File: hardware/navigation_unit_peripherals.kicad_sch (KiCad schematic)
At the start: 25 parts, among them J1 RFPC-SMA28-F, J2 Conn_01x04, U2 BMI088, U3 IIS2MDCTR, U4 MPRLS0025PA00001A, U5 TMP100, U6 24CW1280T-I/OT, U7 MAX-M8Q

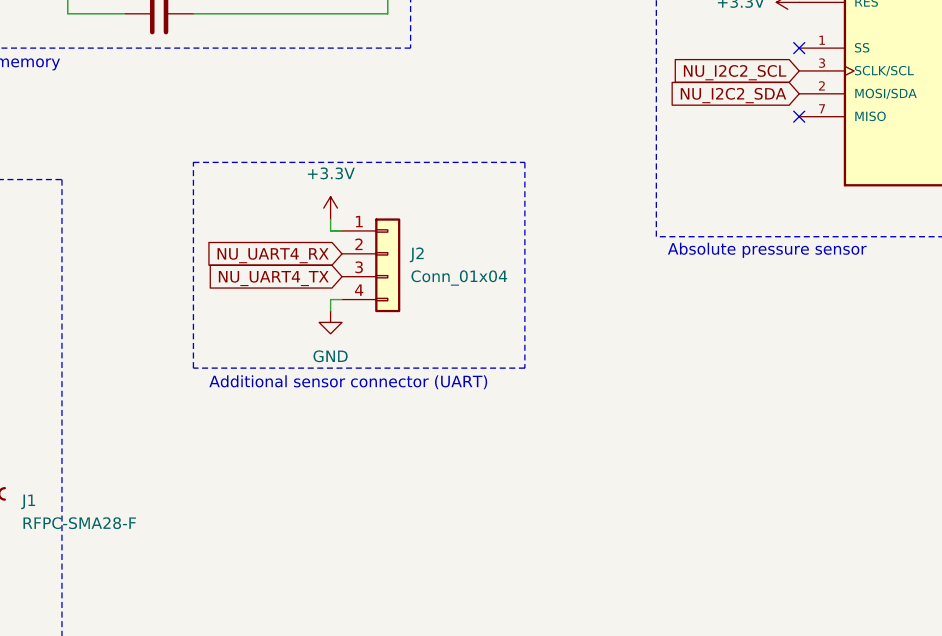
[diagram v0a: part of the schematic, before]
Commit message: schematic and BOM done
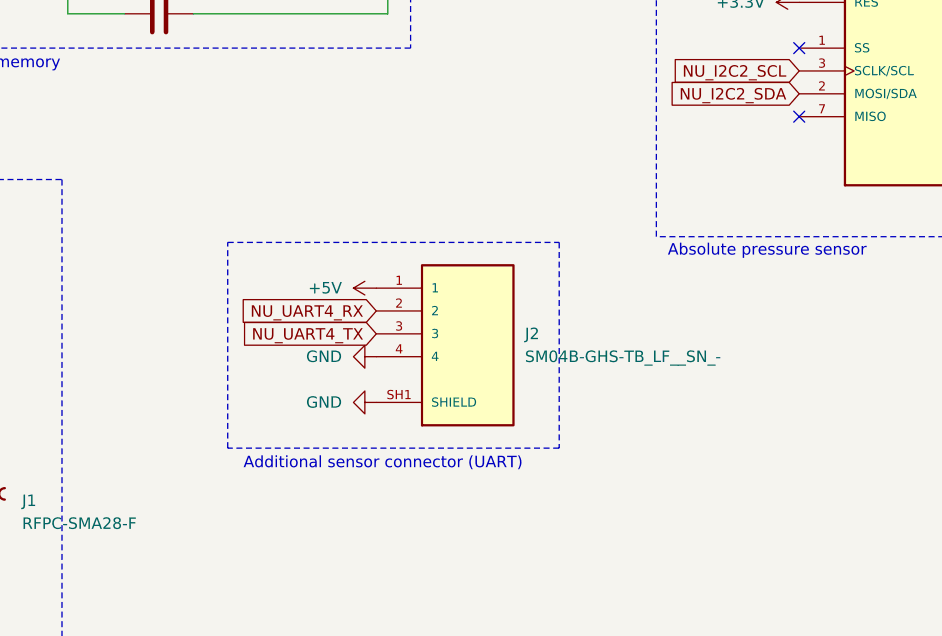
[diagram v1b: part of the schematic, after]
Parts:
- removed J2: Conn_01x04, symbol Connector_Generic:Conn_01x04
- added J2: SM04B-GHS-TB_LF__SN_-, airplane:JST_SM04B-GHS-TB_LF__SN_-, symbol components:SM04B-GHS-TB_LF__SN_-
- C14, C15, C16, C17, C19, C20, C21, C22, C23, C24, C25, C26: footprint (none) -> Capacitor_SMD:C_0603_1608Metric
- C18: footprint (none) -> Capacitor_SMD:C_0805_2012Metric
- J1: footprint RFPC-SMA28-F:GRADCONN_RFPC-SMA28-F -> airplane:GRADCONN_RFPC-SMA28-F; Manufacturer Part Number (none) -> RFPC-SMA28-F
- JP1: footprint (none) -> Jumper:SolderJumper-3_P1.3mm_Open_RoundedPad1.0x1.5mm
- L1: footprint (none) -> Inductor_SMD:L_0603_1608Metric
- R13, R14: footprint (none) -> Resistor_SMD:R_0603_1608Metric
- U2: Manufacturer Part Number (none) -> BMI088
- U3: footprint LGA-12_2X2X0P7_STM -> airplane:LGA-12_2X2X0P7_STM; Manufacturer Part Number (none) -> IIS2MDCTR
- U4: footprint MPRLS0025PA00001A:XDCR_MPRLS0025PA00001A -> airplane:XDCR_MPRLS0025PA00001A; Manufacturer Part Number (none) -> MPRLS0025PA00001A
- U5: Manufacturer Part Number (none) -> TMP100NA/3K
- U6: footprint SOT-23-5_2P9X1P6_MCH -> airplane:SOT-23-5_2P9X1P6_MCH; Manufacturer Part Number (none) -> 24CW1280T-I/OT
- U7: Manufacturer Part Number (none) -> MAX-M8Q
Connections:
- net GND: now also J2.4, J2.SH1 (SHIELD), J2.SH2 (SHIELD)
- net NU_UART4_RX: now also J2.2
- net NU_UART4_TX: now also J2.3
- new net +5V: J2.1
